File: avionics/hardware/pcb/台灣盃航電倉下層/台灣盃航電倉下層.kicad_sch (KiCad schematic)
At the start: 24 parts, among them J1 XT60, J2 XT60, U3 LM2596S-5, U4 LM2596S-5, U5 AMS1117-3.3, U6 AMS1117-3.3

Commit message: Adding AGENTS.MD file
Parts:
- added C3, C4: 22u, symbol Device:C
- added C5, C6: 47u, symbol Device:C
- added U8: ~, symbol MySymbol:2x17排針母座連接
- C1, C2: value 680u -> 100n; footprint Capacitor_SMD:CP_Elec_10x10 -> (none)
- renumbered C6 to C10, C7 to C11, C8 to C12, C9 to C13, C10 to C14, C11 to C15, C12 to C16, C3 to C7, C4 to C8, C5 to C9, U3 to U4, U4 to U5, U5 to U6, U6 to U7
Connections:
- net +BATT_b: now also C4.1, C6.1
- net +BATT_m: now also C3.1, C5.1
- net GND: now also C3.2, C4.2, C5.2, C6.2

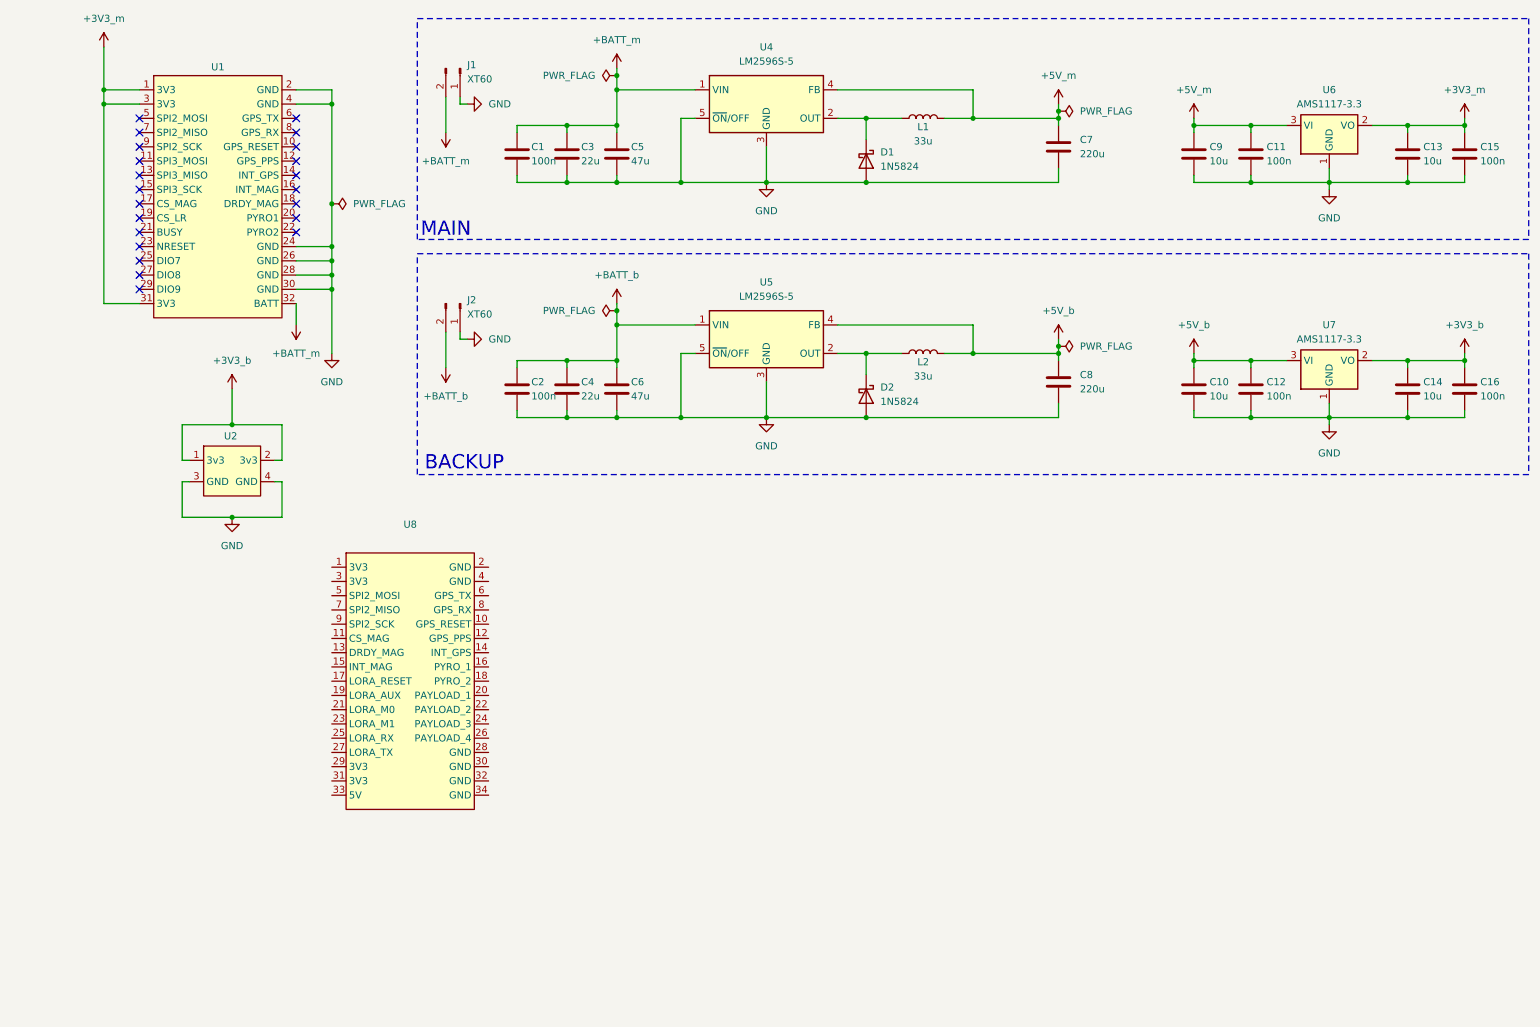
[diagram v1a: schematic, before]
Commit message: 更新下層PCB原理圖
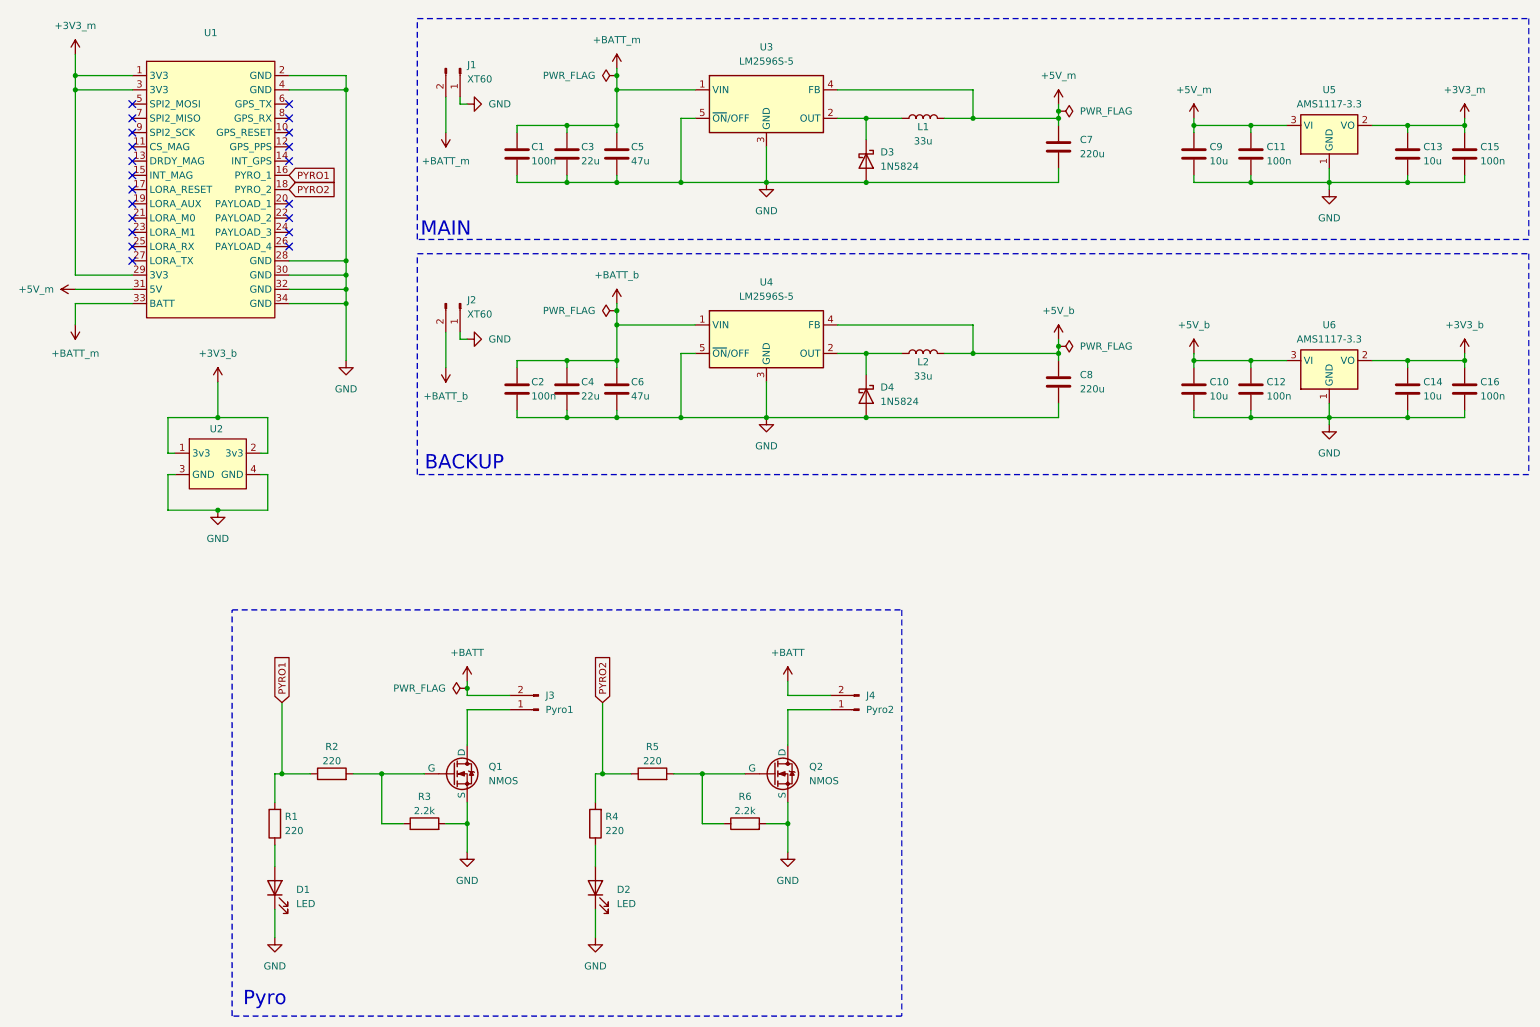
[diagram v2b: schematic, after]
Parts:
- removed U1: ~, symbol MySymbol:2x16排針母座連接
- removed U8: ~, symbol MySymbol:2x17排針母座連接
- added D1, D2: LED, LED_SMD:LED_0805_2012Metric, symbol Device:LED
- added J3: Pyro1, Connector_JST:JST_XH_B2B-XH-A_1x02_P2.50mm_Vertical, symbol Connector:Conn_01x02_Pin
- added J4: Pyro2, Connector_JST:JST_XH_B2B-XH-A_1x02_P2.50mm_Vertical, symbol Connector:Conn_01x02_Pin
- added Q1, Q2: NMOS, Package_TO_SOT_SMD:SOT-223, symbol Simulation_SPICE:NMOS
- added R1, R2, R4, R5: 220, Resistor_SMD:R_0805_2012Metric, symbol Device:R
- added R3, R6: 2.2k, Resistor_SMD:R_0805_2012Metric, symbol Device:R
- added U1: ~, symbol MySymbol:2x17排針母座連接
- renumbered D1 to D3, D2 to D4, U4 to U3, U5 to U4, U6 to U5, U7 to U6
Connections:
- net +3V3_m: now also U1.1 (3V3), U1.29 (3V3), U1.3 (3V3)
- net +5V_m: now also U1.31 (5V)
- net +BATT_m: now also U1.33 (BATT)
- net GND: now also D1.1 (K), D2.1 (K), Q1.3 (S), Q2.3 (S), R3.2, R6.2, U1.2 (GND), U1.28 (GND), U1.30 (GND), U1.32 (GND), U1.34 (GND), U1.4 (GND)
- new net: Q1.2 (G), R2.2, R3.1
- new net: J4.1 (Pin_1), Q2.1 (D)
- new net: D2.2 (A), R4.1
- new net: J3.1 (Pin_1), Q1.1 (D)
- new net: D1.2 (A), R1.1
- new net: Q2.2 (G), R5.2, R6.1
- new net +BATT: J3.2 (Pin_2), J4.2 (Pin_2)
- new net PYRO1: R1.2, R2.1, U1.16 (PYRO_1)
- new net PYRO2: R4.2, R5.1, U1.18 (PYRO_2)
- no-connect marks 22 -> 21
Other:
- note added: "Pyro"
- moved on the sheet: U2
